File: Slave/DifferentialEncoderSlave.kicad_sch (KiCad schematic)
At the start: 29 parts, among them U1 ADM4852, U2 STM32G4A1KEU4, U3 LP5907MFX-3.3, U4 MA730

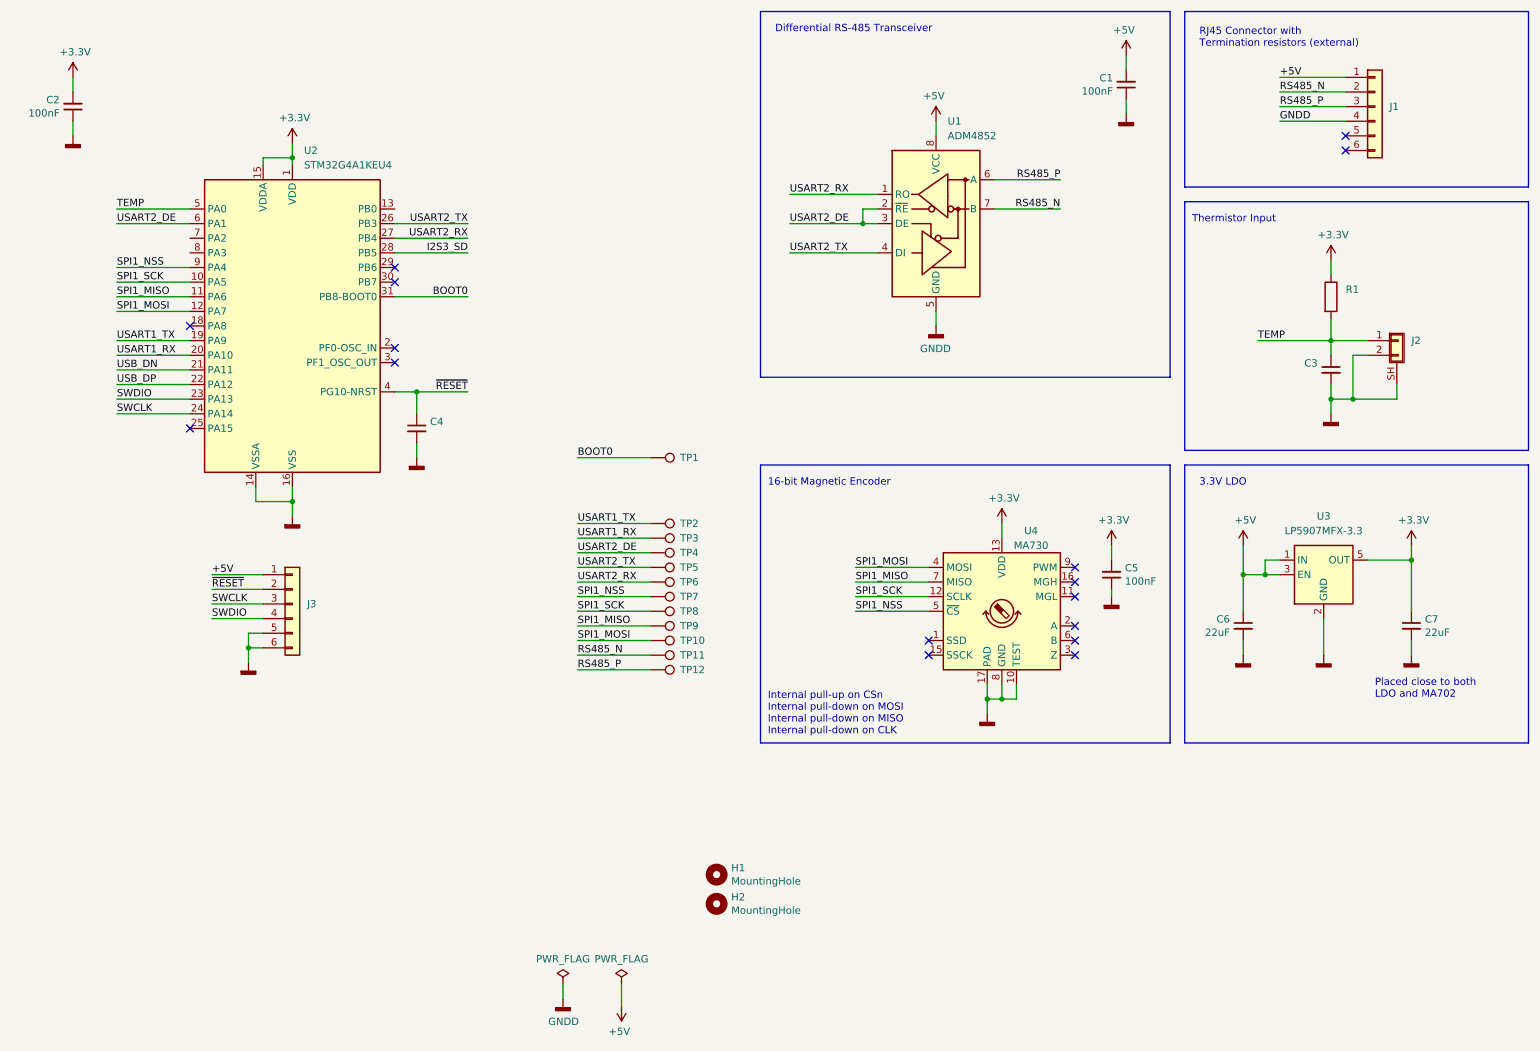
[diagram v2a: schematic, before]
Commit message: Add narrow mounting holes
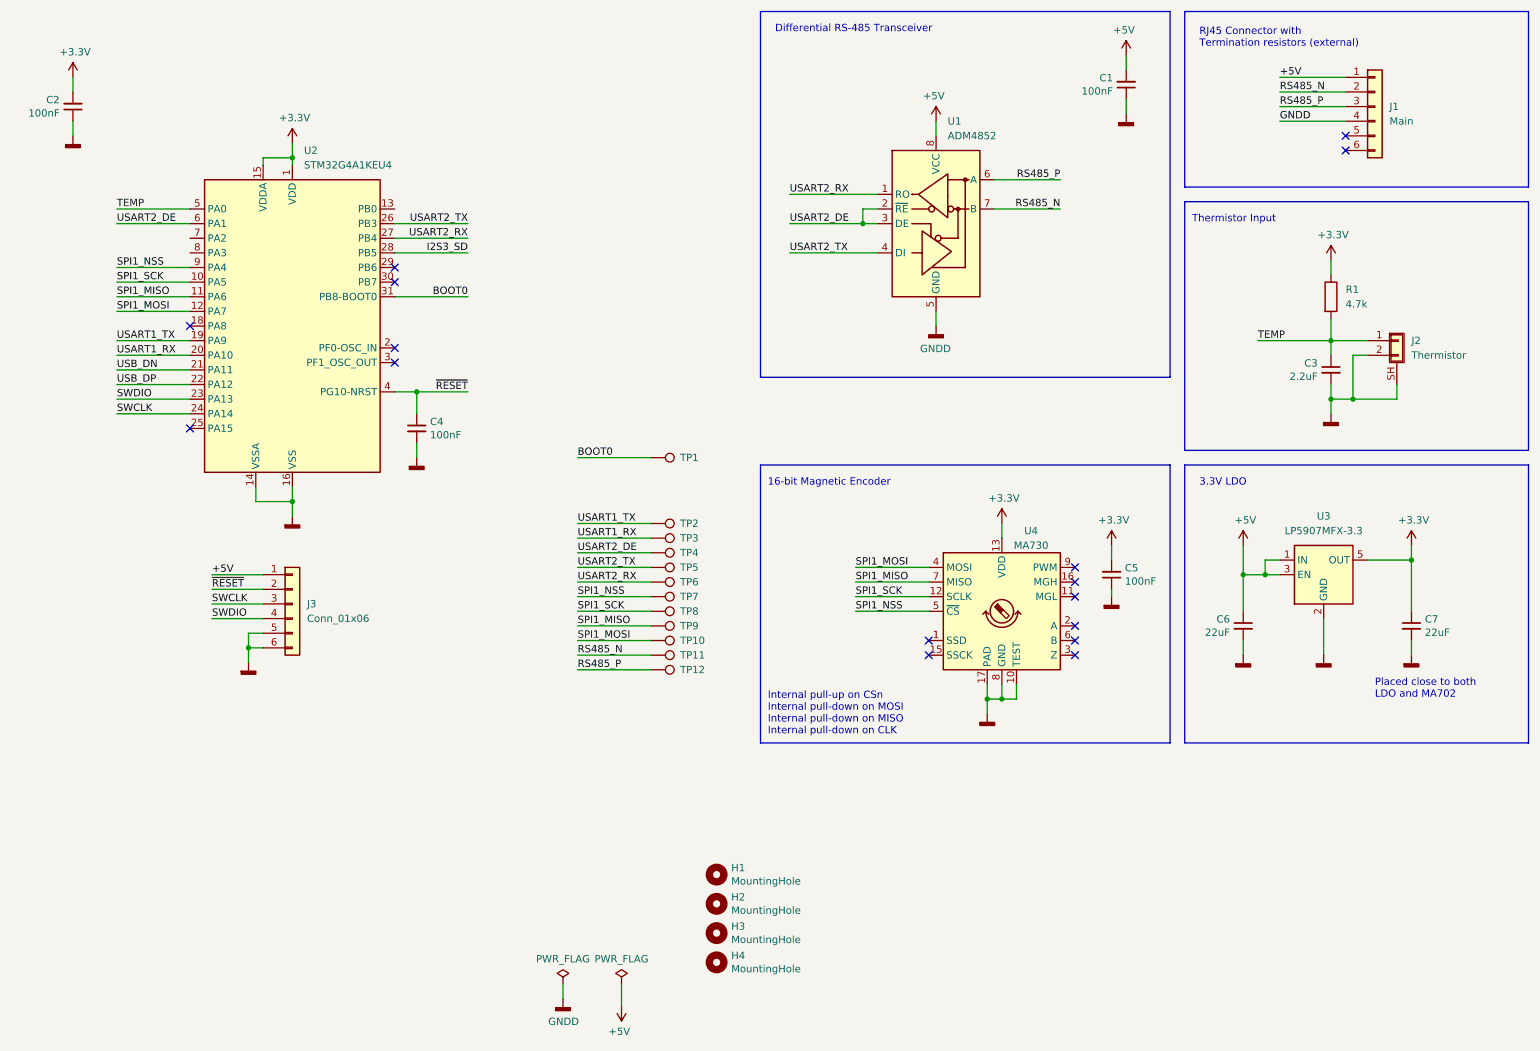
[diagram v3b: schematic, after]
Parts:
- added H3, H4: MountingHole, MountingHole:MountingHole_3mm, symbol Mechanical:MountingHole
- C3: value (none) -> 2.2uF; footprint (none) -> Capacitor_SMD:C_0402_1005Metric
- C4: value (none) -> 100nF; footprint (none) -> Capacitor_SMD:C_0402_1005Metric
- J1: value (none) -> Main
- J2: value (none) -> Thermistor; footprint (none) -> ODrive_KiCad:JST_GH_SM02B
- J3: value (none) -> Conn_01x06; footprint (none) -> Connector:Tag-Connect_TC2030-IDC-NL_2x03_P1.27mm_Vertical
- R1: value (none) -> 4.7k; footprint (none) -> Resistor_SMD:R_0402_1005Metric
- TP1, TP10, TP11, TP12, TP2, TP3, TP4, TP5, TP6, TP7, TP8, TP9: footprint (none) -> ODrive_KiCad:TestPoint_Pad_D1.0mm
- U1: footprint (none) -> Package_CSP:LFCSP-8-1EP_3x3mm_P0.5mm_EP1.45x1.74mm
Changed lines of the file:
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@@
     (pin "32")
     (pin "33")
+    (pin "4")
     (pin "5")
     (pin "6")
-    (pin "4")
     (pin "7")
     (pin "8")
@@
       (effects (font (size 1.27 1.27)) (justify left) hide)
     )
-    (property "Footprint" "" (id 2) (at 127 120.65 0)
+    (property "Footprint" "ODrive_KiCad:TestPoint_Pad_D1.0mm" (id 2) (at 127 120.65 0)
       (effects (font (size 1.27 1.27)) hide)
     )
@@
       (effects (font (size 1.27 1.27)) (justify left))
     )
-    (property "Value" "" (id 1) (at 67.31 121.9199 0)
-      (effects (font (size 1.27 1.27)) (justify left))
-    )
-    (property "Footprint" "" (id 2) (at 64.77 119.38 0)
+    (property "Value" "Conn_01x06" (id 1) (at 67.31 121.9199 0)
+      (effects (font (size 1.27 1.27)) (justify left))
+    )
+    (property "Footprint" "Connector:Tag-Connect_TC2030-IDC-NL_2x03_P1.27mm_Vertical" (id 2) (at 64.77 119.38 0)
       (effects (font (size 1.27 1.27)) hide)
     )
@@
       (effects (font (size 1.27 1.27)) (justify left) hide)
     )
-    (property "Footprint" "" (id 2) (at 127 113.03 0)
+    (property "Footprint" "ODrive_KiCad:TestPoint_Pad_D1.0mm" (id 2) (at 127 113.03 0)
       (effects (font (size 1.27 1.27)) hide)
     )
@@
       (effects (font (size 1.27 1.27)) (justify left))
     )
-    (property "Value" "" (id 1) (at 247.65 67.3099 0)
-      (effects (font (size 1.27 1.27)) (justify left))
-    )
-    (property "Footprint" "" (id 2) (at 243.332 66.04 90)
+    (property "Value" "4.7k" (id 1) (at 247.65 67.3099 0)
+      (effects (font (size 1.27 1.27)) (justify left))
+    )
+    (property "Footprint" "Resistor_SMD:R_0402_1005Metric" (id 2) (at 243.332 66.04 90)
       (effects (font (size 1.27 1.27)) hide)
     )
@@
       (effects (font (size 1.27 1.27)) (justify left) hide)
     )
-    (property "Footprint" "" (id 2) (at 127 99.06 0)
+    (property "Footprint" "ODrive_KiCad:TestPoint_Pad_D1.0mm" (id 2) (at 127 99.06 0)
       (effects (font (size 1.27 1.27)) hide)
     )
@@
       (effects (font (size 1.27 1.27)) (justify left) hide)
     )
-    (property "Footprint" "" (id 2) (at 127 125.73 0)
+    (property "Footprint" "ODrive_KiCad:TestPoint_Pad_D1.0mm" (id 2) (at 127 125.73 0)
       (effects (font (size 1.27 1.27)) hide)
     )
@@
       (effects (font (size 1.27 1.27)) (justify left))
     )
-    (property "Value" "" (id 1) (at 255.27 35.5599 0)
+    (property "Value" "Main" (id 1) (at 255.27 35.5599 0)
       (effects (font (size 1.27 1.27)) (justify left))
     )
@@
       (effects (font (size 1.27 1.27)) (justify left))
     )
-    (property "Value" "" (id 1) (at 242.7986 79.883 0)
-      (effects (font (size 1.27 1.27)) (justify left))
-    )
-    (property "Footprint" "" (id 2) (at 245.11 78.74 0)
+    (property "Value" "2.2uF" (id 1) (at 242.7986 79.883 0)
+      (effects (font (size 1.27 1.27)) (justify left))
+    )
+    (property "Footprint" "Capacitor_SMD:C_0402_1005Metric" (id 2) (at 245.11 78.74 0)
       (effects (font (size 1.27 1.27)) hide)
     )
@@
       (effects (font (size 1.27 1.27)) (justify left) hide)
     )
-    (property "Footprint" "" (id 2) (at 127 110.49 0)
+    (property "Footprint" "ODrive_KiCad:TestPoint_Pad_D1.0mm" (id 2) (at 127 110.49 0)
       (effects (font (size 1.27 1.27)) hide)
     )
@@
       (effects (font (size 1.27 1.27)) (justify left) hide)
     )
-    (property "Footprint" "" (id 2) (at 127 133.35 0)
+    (property "Footprint" "ODrive_KiCad:TestPoint_Pad_D1.0mm" (id 2) (at 127 133.35 0)
       (effects (font (size 1.27 1.27)) hide)
     )
@@
       (effects (font (size 1.27 1.27)) (justify left))
     )
-    (property "Footprint" "" (id 2) (at 176.53 76.2 0)
+    (property "Footprint" "Package_CSP:LFCSP-8-1EP_3x3mm_P0.5mm_EP1.45x1.74mm" (id 2) (at 176.53 76.2 0)
       (effects (font (size 1.27 1.27)) hide)
     )
@@
       (effects (font (size 1.27 1.27)) (justify left) hide)
     )
-    (property "Footprint" "" (id 2) (at 127 130.81 0)
+    (property "Footprint" "ODrive_KiCad:TestPoint_Pad_D1.0mm" (id 2) (at 127 130.81 0)
       (effects (font (size 1.27 1.27)) hide)
     )
@@
     )
     (pin "1")
+  )
+  (symbol (lib_id "Mechanical:MountingHole") (at 138.43 176.53 0) (unit 1)
+    (in_bom yes) (on_board yes)
+    (property "Reference" "H3" (id 0) (at 140.97 175.3616 0)
+      (effects (font (size 1.27 1.27)) (justify left))
+    )
+    (property "Value" "MountingHole" (id 1) (at 140.97 177.673 0)
+      (effects (font (size 1.27 1.27)) (justify left))
+    )
+    (property "Footprint" "MountingHole:MountingHole_3mm" (id 2) (at 138.43 176.53 0)
+      (effects (font (size 1.27 1.27)) hide)
+    )
+    (property "Datasheet" "~" (id 3) (at 138.43 176.53 0)
+      (effects (font (size 1.27 1.27)) hide)
+    )
   )
   (symbol (lib_id "power:+3.3V") (at 26.67 27.94 0) (unit 1)
@@
       (effects (font (size 1.27 1.27)) (justify left))
     )
-    (property "Value" "" (id 1) (at 88.6714 90.043 0)
-      (effects (font (size 1.27 1.27)) (justify left))
-    )
-    (property "Footprint" "" (id 2) (at 86.36 88.9 0)
+    (property "Value" "100nF" (id 1) (at 88.6714 90.043 0)
+      (effects (font (size 1.27 1.27)) (justify left))
+    )
+    (property "Footprint" "Capacitor_SMD:C_0402_1005Metric" (id 2) (at 86.36 88.9 0)
       (effects (font (size 1.27 1.27)) hide)
     )
@@
     (pin "2")
   )
+  (symbol (lib_id "Mechanical:MountingHole") (at 138.43 181.61 0) (unit 1)
+    (in_bom yes) (on_board yes)
+    (property "Reference" "H4" (id 0) (at 140.97 180.4416 0)
+      (effects (font (size 1.27 1.27)) (justify left))
+    )
+    (property "Value" "MountingHole" (id 1) (at 140.97 182.753 0)
+      (effects (font (size 1.27 1.27)) (justify left))
+    )
+    (property "Footprint" "MountingHole:MountingHole_3mm" (id 2) (at 138.43 181.61 0)
+      (effects (font (size 1.27 1.27)) hide)
+    )
+    (property "Datasheet" "~" (id 3) (at 138.43 181.61 0)
+      (effects (font (size 1.27 1.27)) hide)
+    )
+  )
   (symbol (lib_id "Connector:TestPoint") (at 127 130.81 270) (unit 1)
     (in_bom yes) (on_board yes) (fields_autoplaced)
@@
       (effects (font (size 1.27 1.27)) (justify left) hide)
     )
-    (property "Footprint" "" (id 2) (at 127 135.89 0)
+    (property "Footprint" "ODrive_KiCad:TestPoint_Pad_D1.0mm" (id 2) (at 127 135.89 0)
       (effects (font (size 1.27 1.27)) hide)
     )
@@
       (effects (font (size 1.27 1.27)) (justify left) hide)
     )
-    (property "Footprint" "" (id 2) (at 127 128.27 0)
+    (property "Footprint" "ODrive_KiCad:TestPoint_Pad_D1.0mm" (id 2) (at 127 128.27 0)
       (effects (font (size 1.27 1.27)) hide)
     )
@@
       (effects (font (size 1.27 1.27)) (justify left) hide)
     )
-    (property "Footprint" "" (id 2) (at 127 123.19 0)
+    (property "Footprint" "ODrive_KiCad:TestPoint_Pad_D1.0mm" (id 2) (at 127 123.19 0)
       (effects (font (size 1.27 1.27)) hide)
     )
@@
       (effects (font (size 1.27 1.27)) (justify left) hide)
     )
-    (property "Footprint" "" (id 2) (at 127 118.11 0)
+    (property "Footprint" "ODrive_KiCad:TestPoint_Pad_D1.0mm" (id 2) (at 127 118.11 0)
       (effects (font (size 1.27 1.27)) hide)
     )
@@
       (effects (font (size 1.27 1.27)) (justify left))
     )
-    (property "Value" "" (id 1) (at 259.08 76.1999 0)
-      (effects (font (size 1.27 1.27)) (justify left))
-    )
-    (property "Footprint" "" (id 2) (at 256.54 73.66 0)
+    (property "Value" "Thermistor" (id 1) (at 259.08 76.1999 0)
+      (effects (font (size 1.27 1.27)) (justify left))
+    )
+    (property "Footprint" "ODrive_KiCad:JST_GH_SM02B" (id 2) (at 256.54 73.66 0)
       (effects (font (size 1.27 1.27)) hide)
     )
@@
       (effects (font (size 1.27 1.27)) (justify left) hide)
     )
-    (property "Footprint" "" (id 2) (at 127 115.57 0)
+    (property "Footprint" "ODrive_KiCad:TestPoint_Pad_D1.0mm" (id 2) (at 127 115.57 0)
       (effects (font (size 1.27 1.27)) hide)
     )
@@
       (reference "H2") (unit 1) (value "MountingHole") (footprint "MountingHole:MountingHole_3mm")
     )
+    (path "/8a61e2f2-3716-44c4-b12c-058a496def9b"
+      (reference "H3") (unit 1) (value "MountingHole") (footprint "MountingHole:MountingHole_3mm")
+    )
+    (path "/a52f6e08-f34e-4095-832d-e87ac0e56f92"
+      (reference "H4") (unit 1) (value "MountingHole") (footprint "MountingHole:MountingHole_3mm")
+    )
     (path "/4f2b94ef-9676-46ea-9115-5b243d8c3109"

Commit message: Add RS485 termination resistor
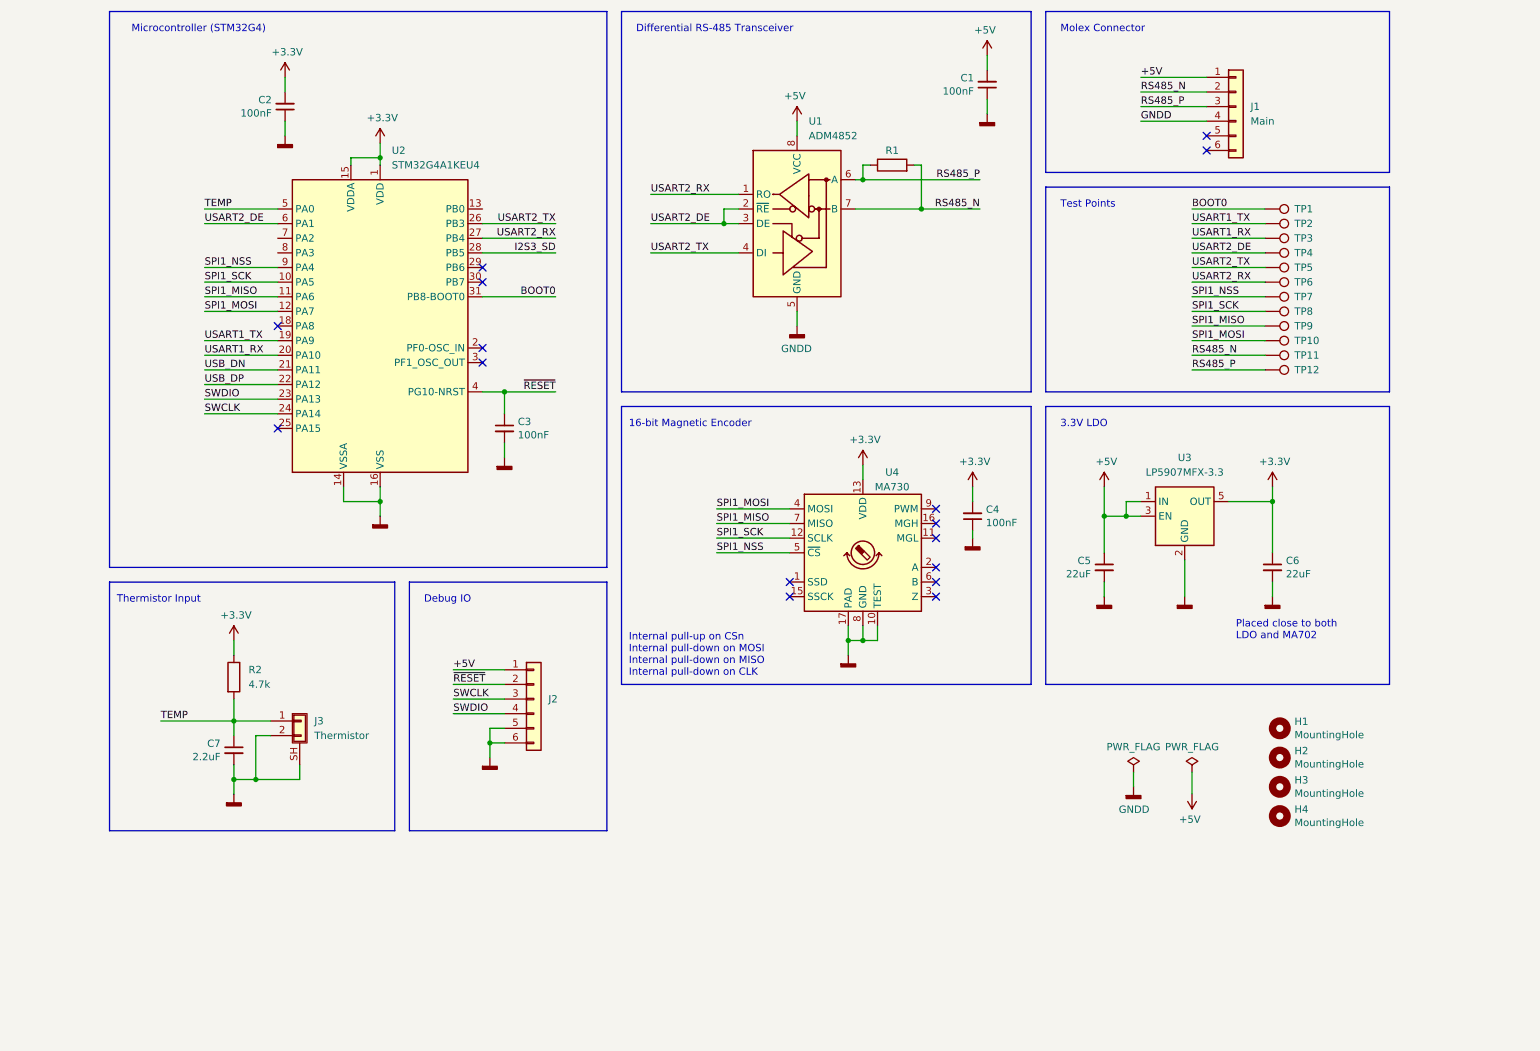
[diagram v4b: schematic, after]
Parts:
- added R1: (no value), Resistor_SMD:R_0402_1005Metric, symbol Device:R
- J2: renamed from J3; value Conn_01x06 -> (none)
- renumbered C4 to C3, C5 to C4, C6 to C5, C7 to C6, C3 to C7, J2 to J3, R1 to R2
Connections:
- net RS485_N: now also R1.2
- net RS485_P: now also R1.1
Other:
- note added: "Debug IO"
- note added: "Microcontroller (STM32G4)"
- note added: "Molex Connector"
- note added: "Test Points"
- note removed: "RJ45 Connector with Termination resistors (external)"
- moved on the sheet: C1, C2, C3, C4, C5, C6, C7, H1, H2, H3, H4, J1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
